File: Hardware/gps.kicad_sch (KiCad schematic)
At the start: 6 parts, among them J10 Conn_Coaxial, U19 MAX-M10S

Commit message: v3 hardware start
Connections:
- net PPS: now reaches U19.4 (TIMEPULSE)
- no-connect marks 5 -> 4

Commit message: replaced efuse with ina219
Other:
- note added: "0x42"
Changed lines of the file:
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@@
+		)
+	)
+	(text "0x42"
+		(exclude_from_sim no)
+		(at 124.714 75.692 0)
+		(effects
+			(font
+				(size 1.27 1.27)
+			)
 		)
 	)

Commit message: Ordering v3
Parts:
- added E1: SparkGap, iclr:Spark_Gap, symbol Device:SparkGap
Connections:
- net GND: now also E1.2
- net at J10.1 (In), L4.2, U19.11 (RF_IN): now also E1.1
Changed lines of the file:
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@@
 	(paper "A4")
+	(junction
+		(at 156.21 58.42)
+		(diameter 0)
+		(color 0 0 0 0)
+	)
 	(junction
 		(at 156.21 76.2)
@@
 	)
 	(junction
+		(at 156.21 60.96)
+		(diameter 0)
+		(color 0 0 0 0)
+	)
+	(junction
 		(at 139.7 115.57)
 		(diameter 0)
 		(color 0 0 0 0)
 	)
-	(junction
-		(at 156.21 59.69)
-		(diameter 0)
-		(color 0 0 0 0)
-	)
 	(no_connect
 		(at 154.94 107.95)
@@
 	(wire
 		(pts
-			(xy 171.45 59.69) (xy 171.45 96.52)
+			(xy 171.45 60.96) (xy 171.45 96.52)
 		)
 		(stroke
@@
 	(wire
 		(pts
-			(xy 156.21 59.69) (xy 171.45 59.69)
+			(xy 156.21 60.96) (xy 171.45 60.96)
 		)
 		(stroke
@@
 	(wire
 		(pts
+			(xy 156.21 58.42) (xy 156.21 57.15)
+		)
+		(stroke
+			(width 0)
+			(type default)
+		)
+	)
+	(wire
+		(pts
 			(xy 156.21 73.66) (xy 156.21 76.2)
 		)
@@
 	(wire
 		(pts
-			(xy 156.21 59.69) (xy 156.21 57.15)
-		)
-		(stroke
-			(width 0)
-			(type default)
-		)
-	)
-	(wire
-		(pts
 			(xy 139.7 76.2) (xy 139.7 78.74)
 		)
@@
 	(wire
 		(pts
-			(xy 156.21 60.96) (xy 156.21 59.69)
+			(xy 156.21 58.42) (xy 156.21 60.96)
 		)
 		(stroke
@@
 			)
 			(justify left)
+		)
+	)
+	(symbol
+		(lib_id "power:GND")
+		(at 166.37 58.42 0)
+		(unit 1)
+		(exclude_from_sim no)
+		(in_bom yes)
+		(on_board yes)
+		(dnp no)
+		(property "Reference" "#PWR0125"
+			(at 166.37 64.77 0)
+			(effects
+				(font
+					(size 1.27 1.27)
+				)
+				(hide yes)
+			)
+		)
+		(property "Value" "GND"
+			(at 166.497 62.8142 0)
+			(effects
+				(font
+					(size 1.27 1.27)
+				)
+			)
+		)
+		(property "Footprint" ""
+			(at 166.37 58.42 0)
+			(effects
+				(font
+					(size 1.27 1.27)
+				)
+				(hide yes)
+			)
+		)
+		(property "Datasheet" ""
+			(at 166.37 58.42 0)
+			(effects
+				(font
+					(size 1.27 1.27)
+				)
+				(hide yes)
+			)
+		)
+		(property "Description" ""
+			(at 166.37 58.42 0)
+			(effects
+				(font
+					(size 1.27 1.27)
+				)
+				(hide yes)
+			)
+		)
+		(pin "1"
+		)
+		(instances
+			(project "PickleRick"
+				(path "/e63e39d7-6ac0-4ffd-8aa3-1841a4541b55/53a382a5-9123-45f3-a2e9-3b2de6ca541d"
+					(reference "#PWR0125")
+					(unit 1)
+				)
+			)
 		)
 	)
@@
 					(unit 1)
 				)
+			)
+		)
+	)
+	(symbol
+		(lib_id "Device:SparkGap")
+		(at 161.29 58.42 0)
+		(unit 1)
+		(exclude_from_sim no)
+		(in_bom yes)
+		(on_board yes)
+		(dnp no)
+		(fields_autoplaced yes)
+		(property "Reference" "E1"
+			(at 161.29 53.34 0)
+			(effects
+				(font
+					(size 1.27 1.27)
+				)
+			)
+		)
+		(property "Value" "SparkGap"
+			(at 161.29 55.88 0)
+			(effects
+				(font
+					(size 1.27 1.27)
+				)
+			)
+		)
+		(property "Footprint" "iclr:Spark_Gap"
+			(at 161.29 60.198 0)
+			(effects
+				(font
+					(size 1.27 1.27)
+				)
+				(hide yes)
+			)
+		)
+		(property "Datasheet" "~"
+			(at 161.29 58.42 90)
+			(effects
+				(font
+					(size 1.27 1.27)
+				)
+				(hide yes)
+			)
+		)
+		(property "Description" "Spark gap"
+			(at 161.29 58.42 0)
+			(effects
+				(font
+					(size 1.27 1.27)
+				)
+				(hide yes)
+			)
+		)
+		(pin "1"
+		)
+		(pin "2"
+		)
+		(instances
+			(project ""
+				(path "/e63e39d7-6ac0-4ffd-8aa3-1841a4541b55/53a382a5-9123-45f3-a2e9-3b2de6ca541d"
+					(reference "E1")
+					(unit 1)
+				)

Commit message: Full v3 Pickle 3d model
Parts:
- U19: footprint RF_GPS:ublox_MAX -> iclr:ublox_MAX
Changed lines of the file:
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@@
 			)
 		)
-		(property "Footprint" "RF_GPS:ublox_MAX"
+		(property "Footprint" "iclr:ublox_MAX"
 			(at 149.86 113.03 0)
 			(effects

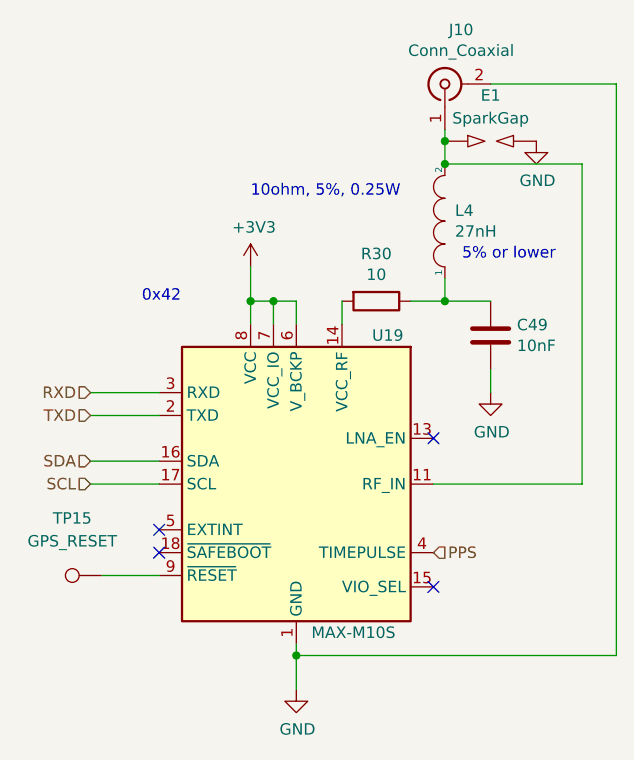
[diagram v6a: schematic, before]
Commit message: cleaned up schematic and bom
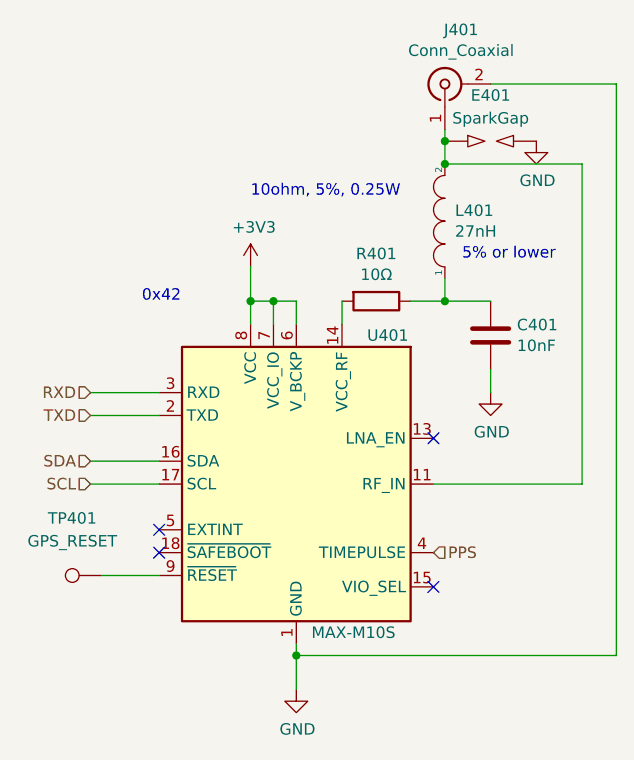
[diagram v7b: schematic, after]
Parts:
- E401: renamed from E1; now left out of the parts list
- R401: renamed from R30; value 10 -> 10Ω
- TP401: renamed from TP15; now left out of the parts list
- renumbered C49 to C401, J10 to J401, L4 to L401, U19 to U401
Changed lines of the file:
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@@
 (kicad_sch
-	(version 20231120)
+	(version 20250114)
 	(generator "eeschema")
-	(generator_version "8.0")
+	(generator_version "9.0")
 	(paper "A4")
+	(text "5% or lower"
+		(exclude_from_sim no)
+		(at 158.115 71.755 0)
+		(effects
+			(font
+				(size 1.27 1.27)
+			)
+			(justify left bottom)
+		)
+	)
+	(text "0x42"
+		(exclude_from_sim no)
+		(at 124.714 75.692 0)
+		(effects
+			(font
+				(size 1.27 1.27)
+			)
+		)
+	)
+	(text "10ohm, 5%, 0.25W"
+		(exclude_from_sim no)
+		(at 134.62 64.77 0)
+		(effects
+			(font
+				(size 1.27 1.27)
+			)
+			(justify left bottom)
+		)
+	)
 	(junction
 		(at 156.21 58.42)
@@
 			(width 0)
 			(type default)
-		)
-	)
-	(text "5% or lower"
-		(exclude_from_sim no)
-		(at 158.115 71.755 0)
-		(effects
-			(font
-				(size 1.27 1.27)
-			)
-			(justify left bottom)
-		)
-	)
-	(text "0x42"
-		(exclude_from_sim no)
-		(at 124.714 75.692 0)
-		(effects
-			(font
-				(size 1.27 1.27)
-			)
-		)
-	)
-	(text "10ohm, 5%, 0.25W"
-		(exclude_from_sim no)
-		(at 134.62 64.77 0)
-		(effects
-			(font
-				(size 1.27 1.27)
-			)
-			(justify left bottom)
 		)
 	)
@@
 		(on_board yes)
 		(dnp no)
-		(property "Reference" "#PWR0125"
+		(property "Reference" "#PWR0404"
 			(at 166.37 64.77 0)
 			(effects
@@
 			(project "PickleRick"
 				(path "/e63e39d7-6ac0-4ffd-8aa3-1841a4541b55/53a382a5-9123-45f3-a2e9-3b2de6ca541d"
-					(reference "#PWR0125")
+					(reference "#PWR0404")
 					(unit 1)
 				)
@@
 		(on_board yes)
 		(dnp no)
-		(property "Reference" "J10"
+		(property "Reference" "J401"
 			(at 158.0134 46.0502 90)
 			(effects
@@
 			)
 		)
-		(property "Datasheet" " ~"
+		(property "Datasheet" "~"
 			(at 156.21 52.07 0)
 			(effects
@@
 			(project "PickleRick"
 				(path "/e63e39d7-6ac0-4ffd-8aa3-1841a4541b55/53a382a5-9123-45f3-a2e9-3b2de6ca541d"
-					(reference "J10")
+					(reference "J401")
 					(unit 1)
 				)
@@
 		(on_board yes)
 		(dnp no)
-		(property "Reference" "#PWR0119"
+		(property "Reference" "#PWR0402"
 			(at 139.7 125.73 0)
 			(effects
@@
 			(project "PickleRick"
 				(path "/e63e39d7-6ac0-4ffd-8aa3-1841a4541b55/53a382a5-9123-45f3-a2e9-3b2de6ca541d"
-					(reference "#PWR0119")
+					(reference "#PWR0402")
 					(unit 1)
 				)
@@
 		(unit 1)
 		(exclude_from_sim no)
-		(in_bom yes)
+		(in_bom no)
 		(on_board yes)
 		(dnp no)
 		(fields_autoplaced yes)
-		(property "Reference" "TP15"
+		(property "Reference" "TP401"
 			(at 114.808 100.33 90)
 			(effects
@@
 			(project "PickleRick"
 				(path "/e63e39d7-6ac0-4ffd-8aa3-1841a4541b55/53a382a5-9123-45f3-a2e9-3b2de6ca541d"
-					(reference "TP15")
+					(reference "TP401")
 					(unit 1)
 				)
@@
 		(unit 1)
 		(exclude_from_sim no)
-		(in_bom yes)
+		(in_bom no)
 		(on_board yes)
 		(dnp no)
 		(fields_autoplaced yes)
-		(property "Reference" "E1"
+		(property "Reference" "E401"
 			(at 161.29 53.34 0)
 			(effects
@@
 		)
 		(instances
-			(project ""
+			(project "PickleRick"
 				(path "/e63e39d7-6ac0-4ffd-8aa3-1841a4541b55/53a382a5-9123-45f3-a2e9-3b2de6ca541d"
-					(reference "E1")
+					(reference "E401")
 					(unit 1)
 				)
@@
 		(on_board yes)
 		(dnp no)
-		(property "Reference" "#PWR0118"
+		(property "Reference" "#PWR0401"
 			(at 134.62 76.2 0)
 			(effects
@@
 			(project "PickleRick"
 				(path "/e63e39d7-6ac0-4ffd-8aa3-1841a4541b55/53a382a5-9123-45f3-a2e9-3b2de6ca541d"
-					(reference "#PWR0118")
+					(reference "#PWR0401")
 					(unit 1)
 				)
@@
 		(on_board yes)
 		(dnp no)
-		(property "Reference" "L4"
+		(property "Reference" "L401"
 			(at 157.3276 66.1416 90)
 			(effects
@@
 			(project "PickleRick"
 				(path "/e63e39d7-6ac0-4ffd-8aa3-1841a4541b55/53a382a5-9123-45f3-a2e9-3b2de6ca541d"
-					(reference "L4")
+					(reference "L401")
 					(unit 1)
 				)
@@
 		(on_board yes)
 		(dnp no)
-		(property "Reference" "R30"
+		(property "Reference" "R401"
 			(at 148.59 70.9422 90)
 			(effects
@@
 			)
 		)
-		(property "Value" "10"
+		(property "Value" "10Ω"
 			(at 148.59 73.2536 90)
 			(effects
@@
 			(project "PickleRick"
 				(path "/e63e39d7-6ac0-4ffd-8aa3-1841a4541b55/53a382a5-9123-45f3-a2e9-3b2de6ca541d"
-					(reference "R30")
+					(reference "R401")
 					(unit 1)
 				)
@@
 		(on_board yes)
 		(dnp no)
-		(property "Reference" "C49"
+		(property "Reference" "C401"
 			(at 164.211 78.8416 0)
 			(effects
@@
 			(project "PickleRick"
 				(path "/e63e39d7-6ac0-4ffd-8aa3-1841a4541b55/53a382a5-9123-45f3-a2e9-3b2de6ca541d"
-					(reference "C49")
+					(reference "C401")
 					(unit 1)
 				)
@@
 		(on_board yes)
 		(dnp no)
-		(property "Reference" "U19"
+		(property "Reference" "U401"
 			(at 149.86 80.01 0)
 			(effects
@@
 			(project "PickleRick"
 				(path "/e63e39d7-6ac0-4ffd-8aa3-1841a4541b55/53a382a5-9123-45f3-a2e9-3b2de6ca541d"
-					(reference "U19")
+					(reference "U401")
 					(unit 1)
 				)
@@
 		(on_board yes)
 		(dnp no)
-		(property "Reference" "#PWR0120"
+		(property "Reference" "#PWR0403"
 			(at 161.29 92.71 0)
 			(effects
@@
 			(project "PickleRick"
 				(path "/e63e39d7-6ac0-4ffd-8aa3-1841a4541b55/53a382a5-9123-45f3-a2e9-3b2de6ca541d"
-					(reference "#PWR0120")
+					(reference "#PWR0403")
 					(unit 1)
 				)
